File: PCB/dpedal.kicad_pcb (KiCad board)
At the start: 2 copper layers, 154 x 80 mm, 26 parts, among them J1 USB_C_Receptacle_USB2.0, J2 Conn_02x10_Counter_Clockwise, J3 Conn_ARM_JTAG_SWD_10, J4 Conn_01x05, SW1 SW_Push, SW10 SW_Push, SW2 SW_Push, SW3 SW_Push, SW4 SW_Push, SW5 RESET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

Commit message: pcb fixes
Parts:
- moved SW10 0.08 mm to (157.0, 59.9)
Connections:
- U1 pad 1: 3.3V -> unconnected-(U1-VBAT-Pad1)
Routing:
- net GND: track 23.9 -> 25.0 mm
- net 3.3V: track 62.3 -> 61.7 mm, vias 4 -> 3

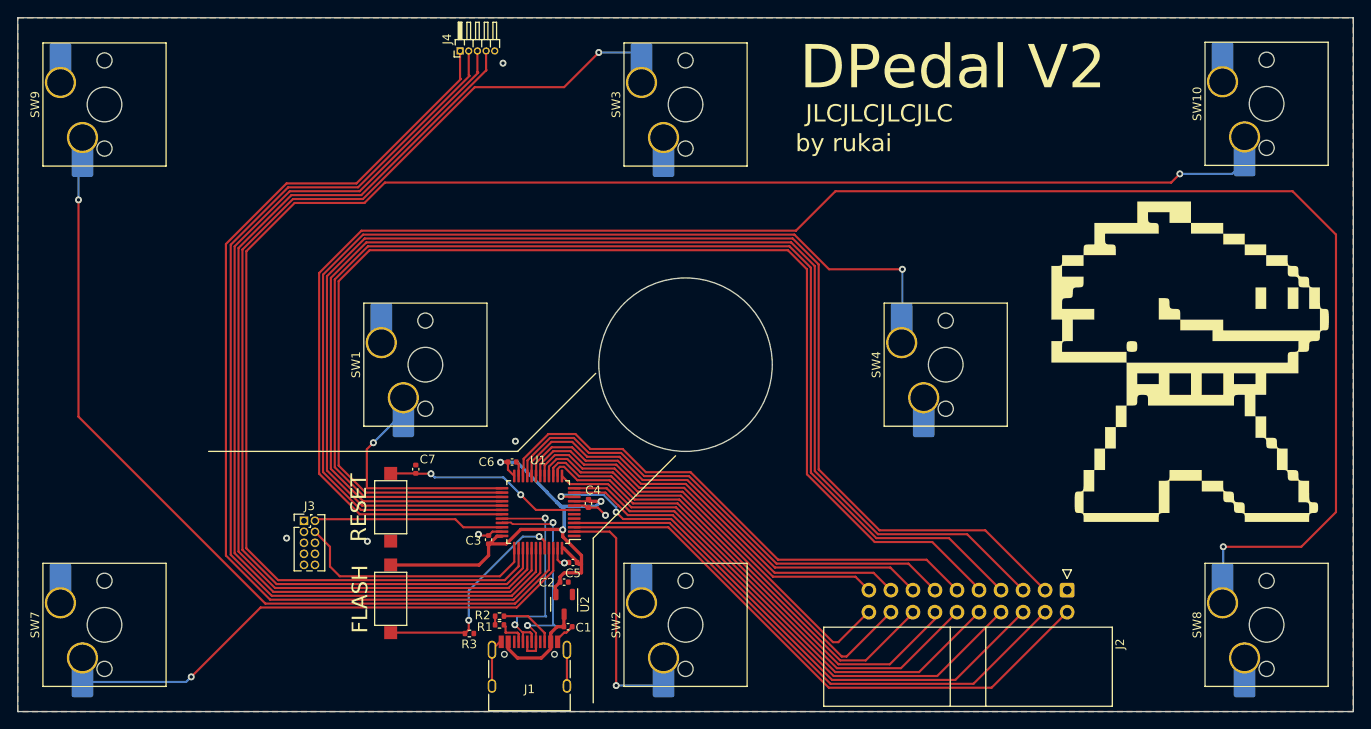
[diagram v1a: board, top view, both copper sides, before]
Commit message: PCB fix drc errors + change pedal headers to 2.54mm
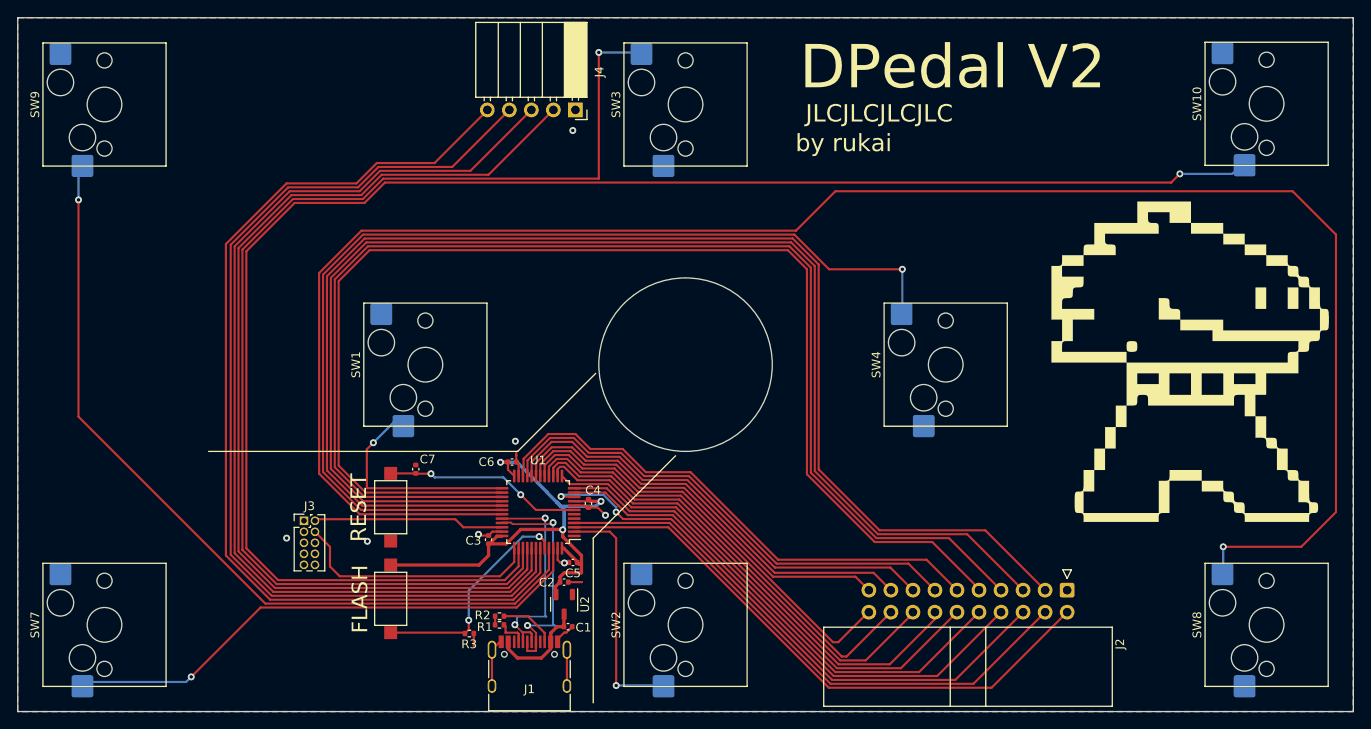
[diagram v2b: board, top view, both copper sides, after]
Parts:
- J4: footprint Connector_PinHeader_1.00mm:PinHeader_1x05_P1.00mm_Horizontal -> Connector_PinSocket_2.54mm:PinSocket_1x05_P2.54mm_Horizontal
- SW1, SW10, SW2, SW3, SW4, SW7, SW8, SW9: footprint Switch_Keyboard_Hotswap_Kailh:SW_Hotswap_Kailh_MX_plated_1.00u -> Switch_Keyboard_Hotswap_Kailh:SW_Hotswap_Kailh_MX
- moved J4 14.9 mm to (77.3, 60.6), turned to -90 degrees
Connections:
- J4 pad 1: PEDAL1 -> GND
- J4 pad 2: PEDAL2 -> PEDAL4
- J4 pad 4: PEDAL4 -> PEDAL2
- J4 pad 5: GND -> PEDAL1
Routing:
- net SW3: track 127.4 -> 135.9 mm
- net GND: track 25.0 -> 29.0 mm
- net PEDAL4: track 112.7 -> 116.3 mm
- net PEDAL3: track 114.0 -> 115.8 mm
- net PEDAL1: track 116.6 -> 115.0 mm
- net SW9: track 96.9 -> 96.2 mm
- net SW2: track 27.8 -> 27.2 mm

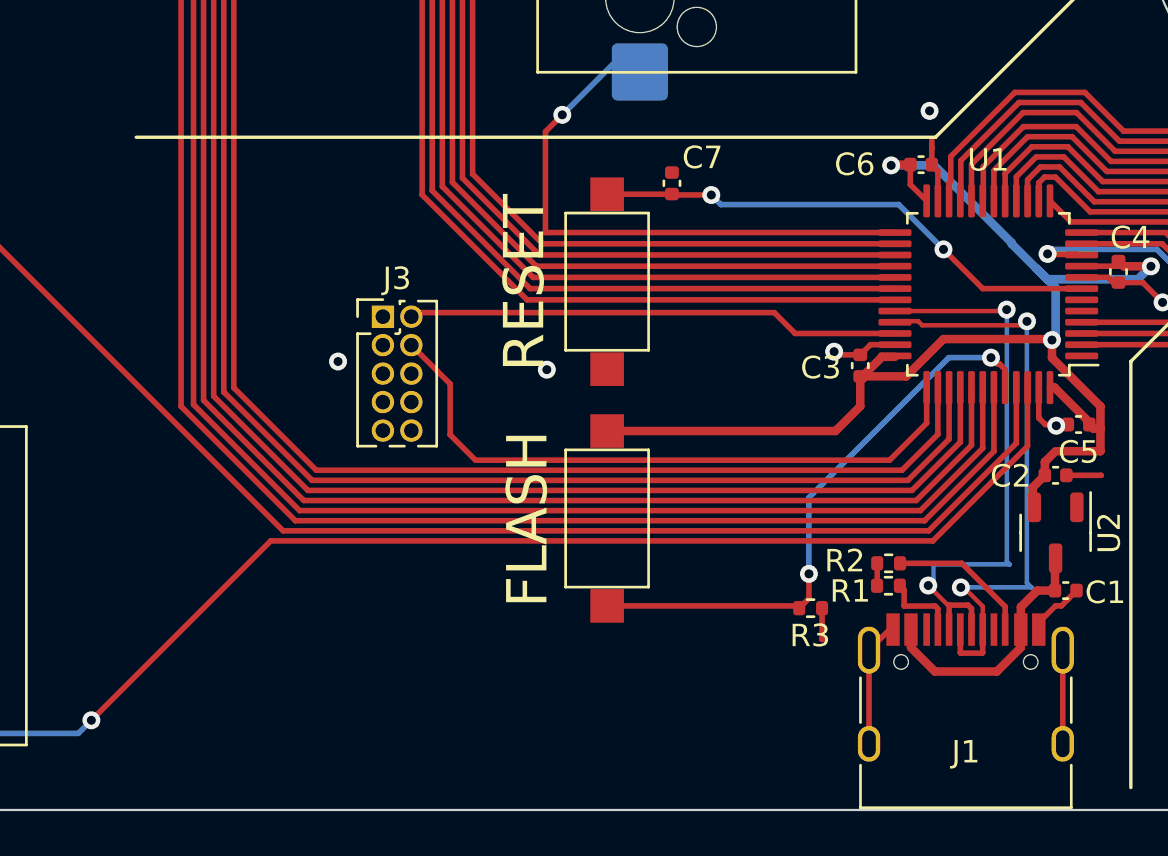
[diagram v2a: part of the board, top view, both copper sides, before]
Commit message: Move reset and flash buttons to bottom of board
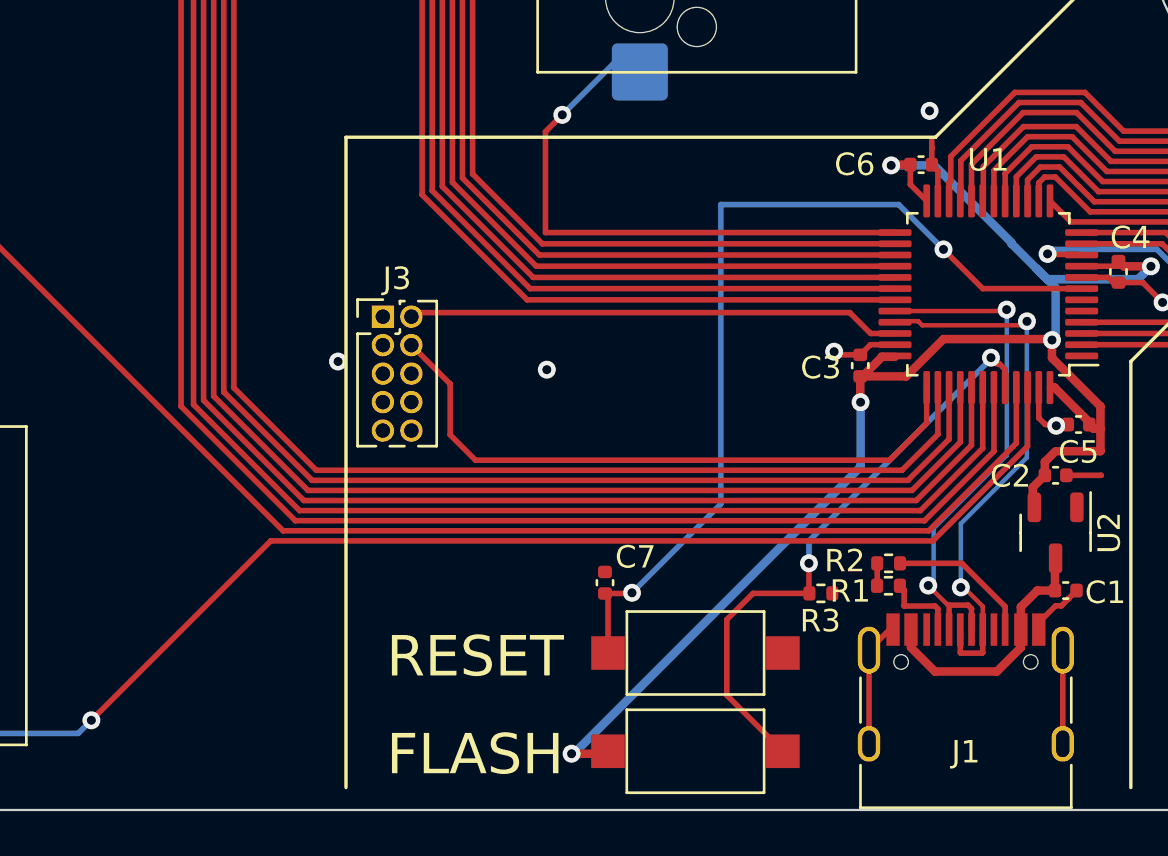
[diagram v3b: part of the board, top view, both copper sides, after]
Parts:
- moved C7 18.1 mm to (55.9, 119.9)
- moved SW5 17.0 mm to (59.9, 123.0), turned to 180 degrees
- moved SW6 11.1 mm to (59.9, 127.4), turned to 0 degrees
- moved R3 0.80 mm to (65.5, 120.3)
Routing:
- net Net-(U1-NRST): track 22.9 -> 40.5 mm
- net 3.3V: track 61.7 -> 72.5 mm, vias 3 -> 5
- net D-: track 25.2 -> 23.1 mm
- net D+: track 26.6 -> 24.6 mm
- net GND: track 29.0 -> 27.6 mm
- net Net-(U1-BOOT0): track 26.1 -> 26.6 mm

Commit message: Move debug port down
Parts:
- moved J3 12.2 mm to (48.7, 119.9), turned to 90 degrees
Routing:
- net SW3: track 135.9 -> 111.5 mm
- net PEDAL3: track 115.8 -> 92.9 mm
- net SW10: track 189.3 -> 166.4 mm
- net PEDAL2: track 115.3 -> 92.4 mm
- net PEDAL4: track 116.3 -> 93.4 mm
- net PEDAL1: track 115.0 -> 92.1 mm
- net SW7: track 62.2 -> 76.6 mm
- net SW9: track 96.2 -> 85.7 mm
- net SWDIO: track 22.0 -> 28.7 mm, vias 0 -> 2
- net SWDCLK: track 28.7 -> 25.7 mm, vias 0 -> 2
- net 3.3V: track 72.5 -> 73.3 mm
- net GND: vias 7 -> 5

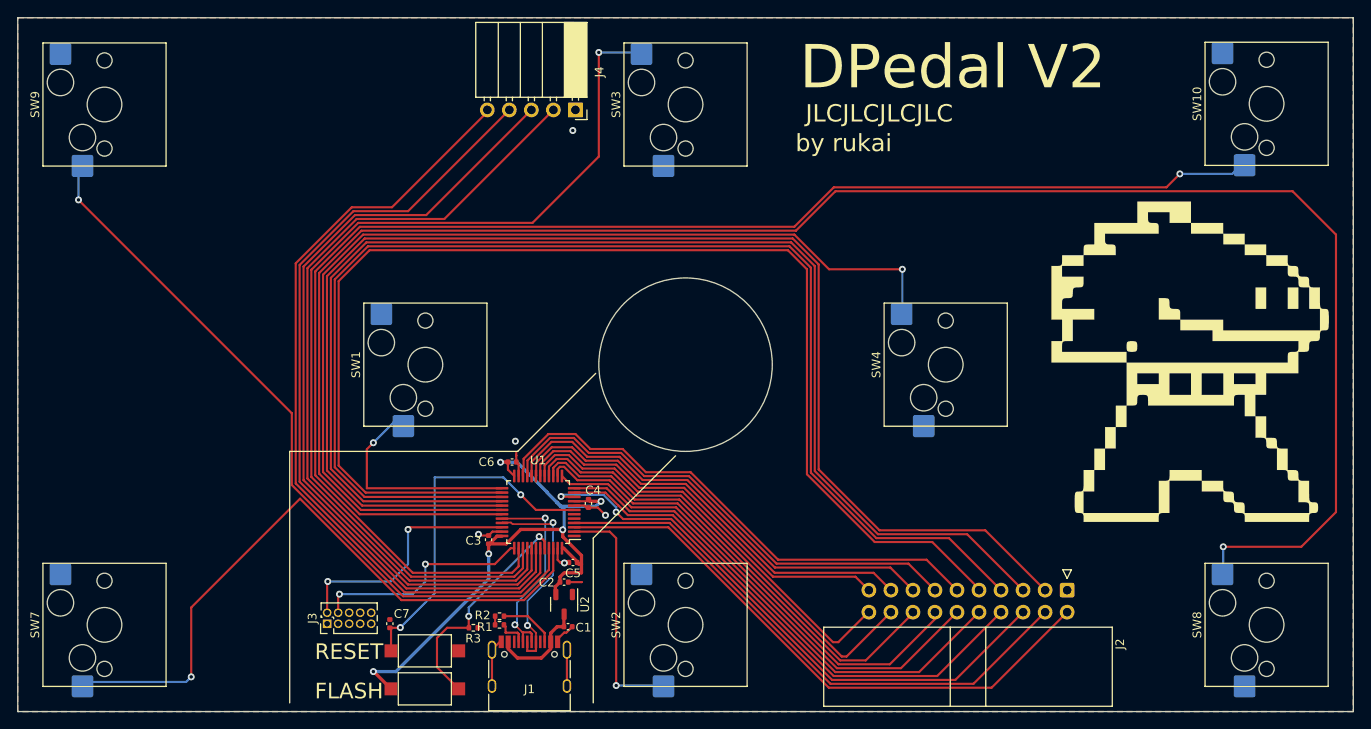
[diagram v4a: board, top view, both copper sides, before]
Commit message: Better align components to shell holes
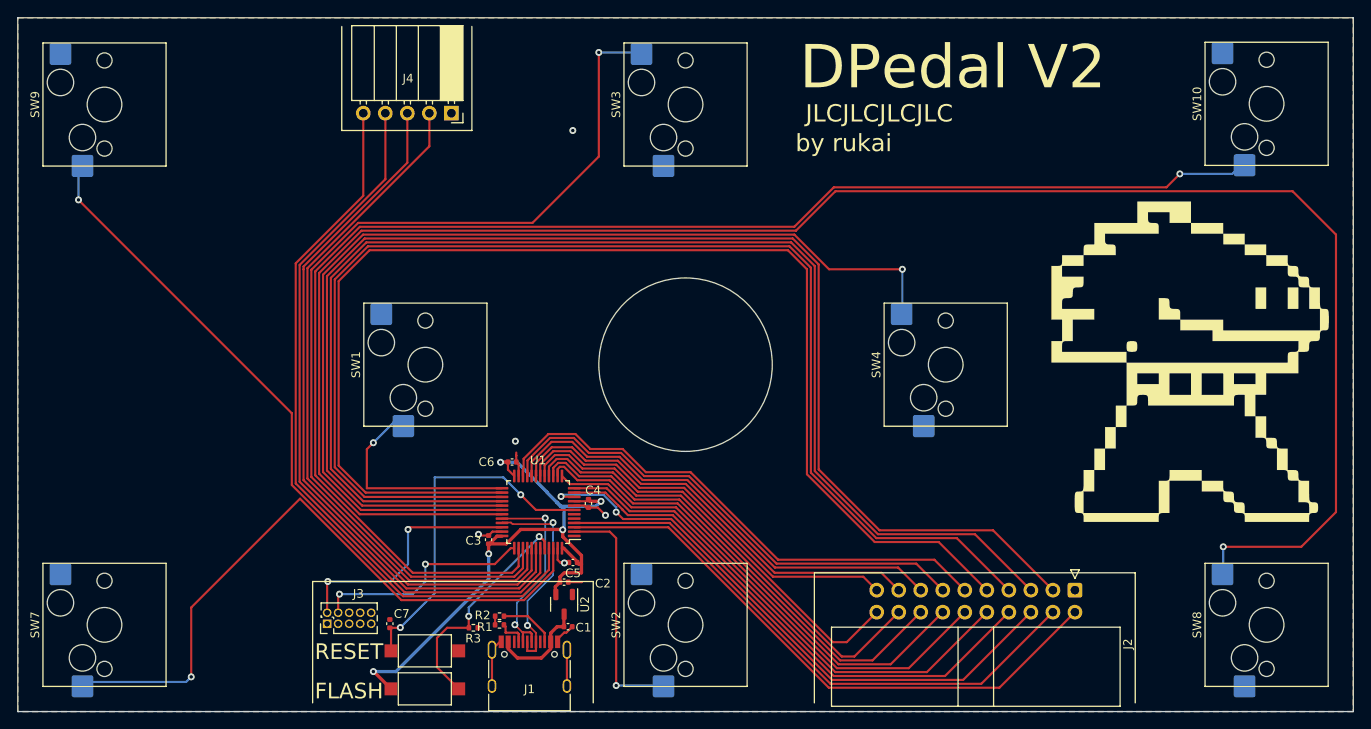
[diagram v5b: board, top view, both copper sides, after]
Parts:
- moved J4 14.3 mm to (63.0, 61.0)
- moved J2 0.90 mm to (134.9, 116.0)
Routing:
- net PEDAL4: track 93.4 -> 81.2 mm
- net PEDAL3: track 92.9 -> 81.8 mm
- net PEDAL2: track 92.4 -> 82.5 mm
- net PEDAL1: track 92.1 -> 83.1 mm
- net EXT15: track 53.6 -> 54.5 mm
- net EXT8: track 61.0 -> 61.9 mm
- net EXT7: track 151.0 -> 151.9 mm
- net EXT6: track 67.1 -> 68.0 mm
- net EXT5: track 155.3 -> 156.2 mm
- net EXT20: track 49.5 -> 50.4 mm
- net EXT12: track 57.4 -> 58.3 mm
- net EXT11: track 60.6 -> 61.5 mm
- net EXT13: track 57.1 -> 58.0 mm
- net EXT4: track 65.4 -> 66.3 mm
- net EXT2: track 68.1 -> 69.0 mm
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
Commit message: Finalize PCB BOM
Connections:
- U1 pad 30: SW4 -> SW8
- U1 pad 31: SW8 -> SW4
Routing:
- net SW8: track 219.6 -> 183.3 mm
- net GND: track 27.6 -> 30.5 mm
- net SW4: track 121.2 -> 122.9 mm

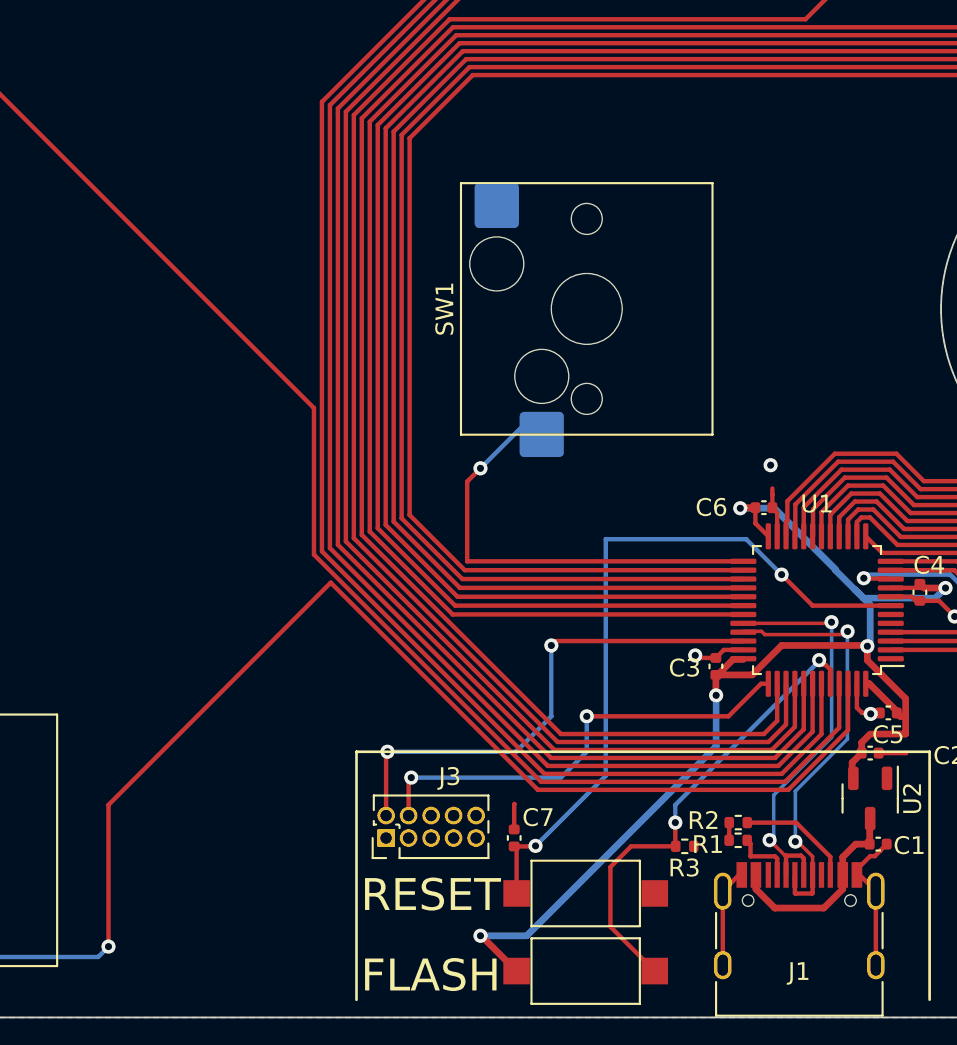
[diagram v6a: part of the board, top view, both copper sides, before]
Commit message: Swap out cortex debug connector for custom 2.54 pinout (2.54 will be much easier to hand solder)
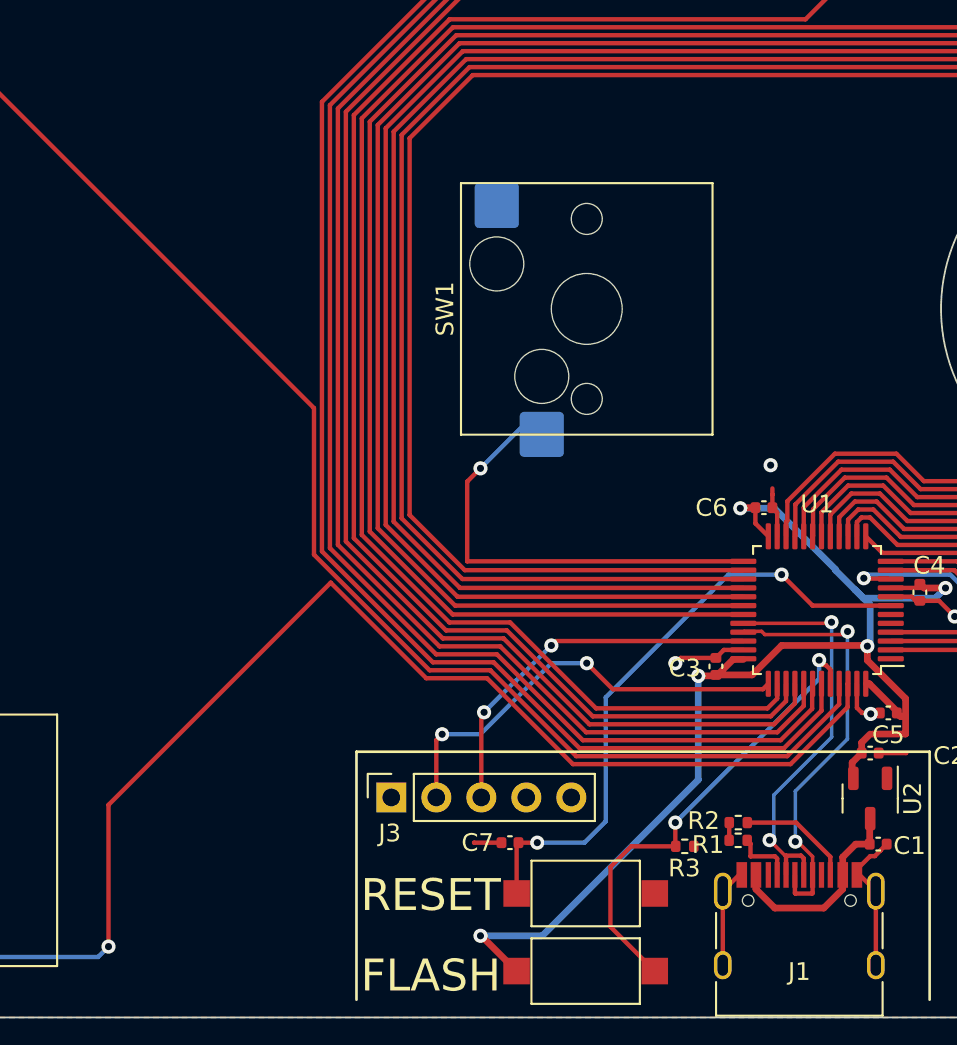
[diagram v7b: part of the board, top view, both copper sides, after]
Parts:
- J3: value Conn_ARM_JTAG_SWD_10 -> Conn_01x05; footprint Connector_PinHeader_1.27mm:PinHeader_2x05_P1.27mm_Vertical -> Connector_PinSocket_2.54mm:PinSocket_1x05_P2.54mm_Vertical
- moved J3 2.31 mm to (49.0, 117.6)
- moved C7 0.36 mm to (55.7, 120.1), turned to 0 degrees
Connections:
- J3 pad 1: unconnected-(J3-VTref-Pad1) -> GND
- J3 pad 2: SWDIO -> SWDCLK
- J3 pad 3: GND -> SWDIO
- J3 pad 4: SWDCLK -> unconnected-(J3-Pin_4-Pad4)
- J3 pad 5: GND -> unconnected-(J3-Pin_5-Pad5)
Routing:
- net SWDIO: track 28.7 -> 21.3 mm
- net Net-(U1-NRST): track 40.5 -> 35.0 mm
- net SW9: track 85.7 -> 83.8 mm
- net SW3: track 111.5 -> 109.5 mm
- net PEDAL4: track 81.2 -> 79.2 mm
- net PEDAL3: track 81.8 -> 79.8 mm
- net PEDAL1: track 83.1 -> 81.1 mm
- net SW7: track 76.6 -> 74.6 mm
- net PEDAL2: track 82.5 -> 80.5 mm
- net SW10: track 166.4 -> 164.5 mm
- net GND: track 30.5 -> 31.8 mm
- net SWDCLK: track 25.7 -> 24.5 mm
- net 3.3V: track 73.3 -> 74.3 mm

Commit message: more final pcb cleanup
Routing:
- net Net-(J1-CC2): track 6.51 -> 7.09 mm
- net D+: track 24.6 -> 24.0 mm
